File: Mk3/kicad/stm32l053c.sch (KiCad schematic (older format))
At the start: 17 parts, among them P1 SWD, U1 STM32L053C8_LQFP48, U2 ADS1015, U3 AP2112, U4 EDGE_SMA, U5 RFM92/95

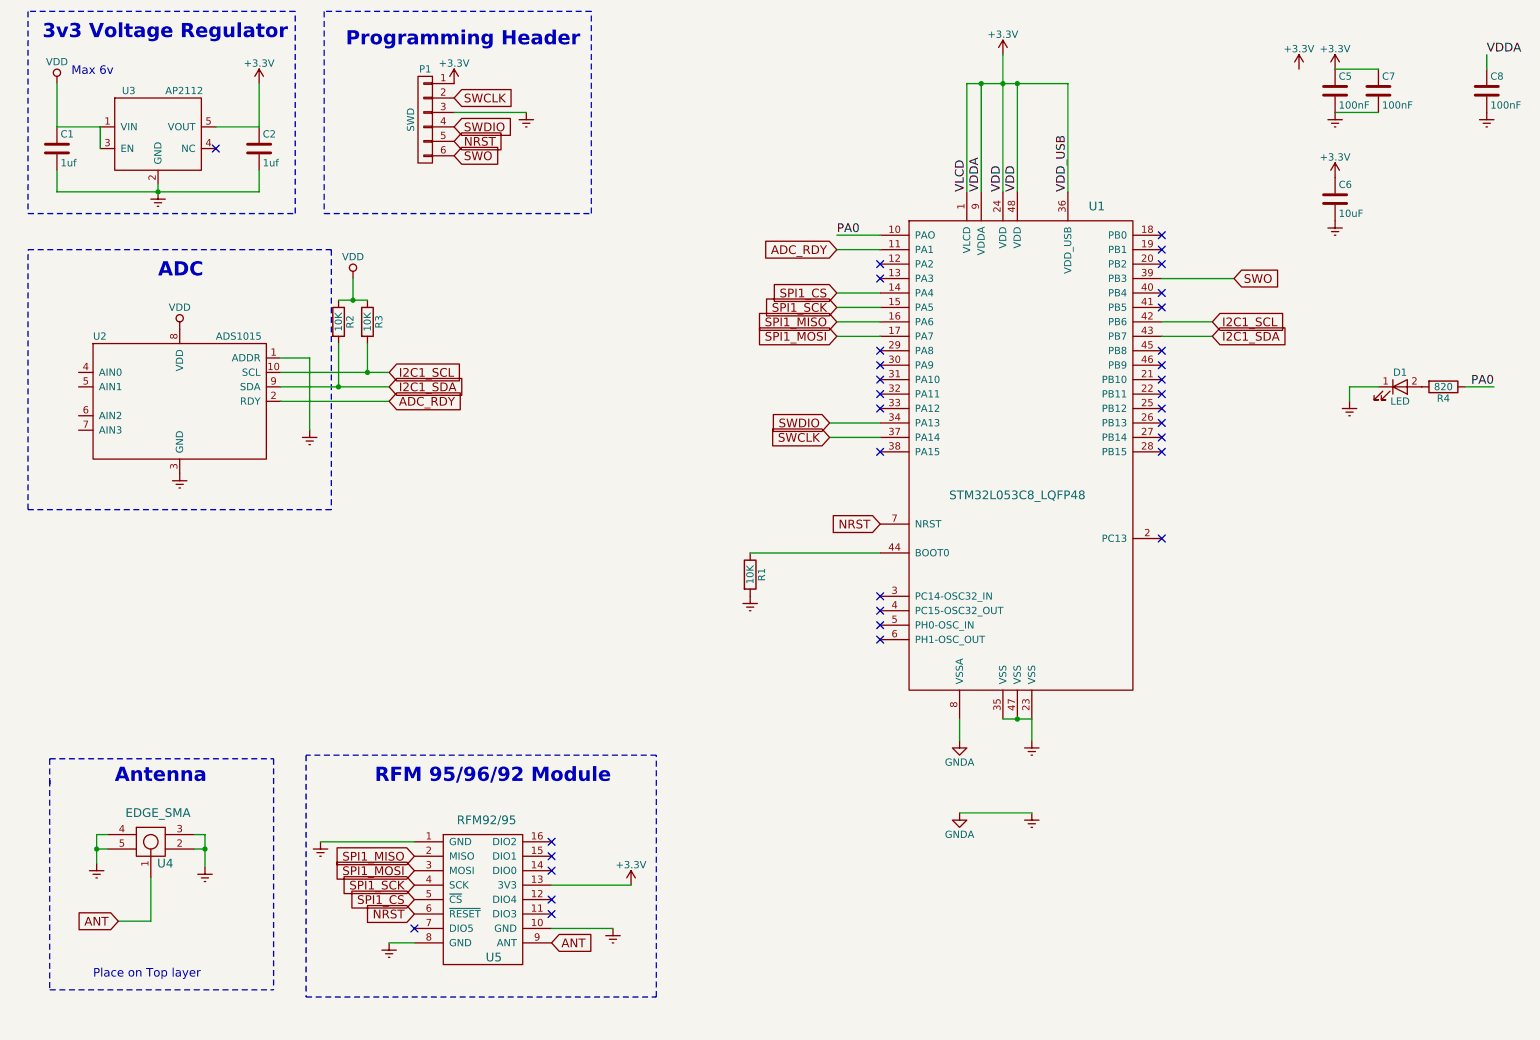
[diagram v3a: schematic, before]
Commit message: ADC connections
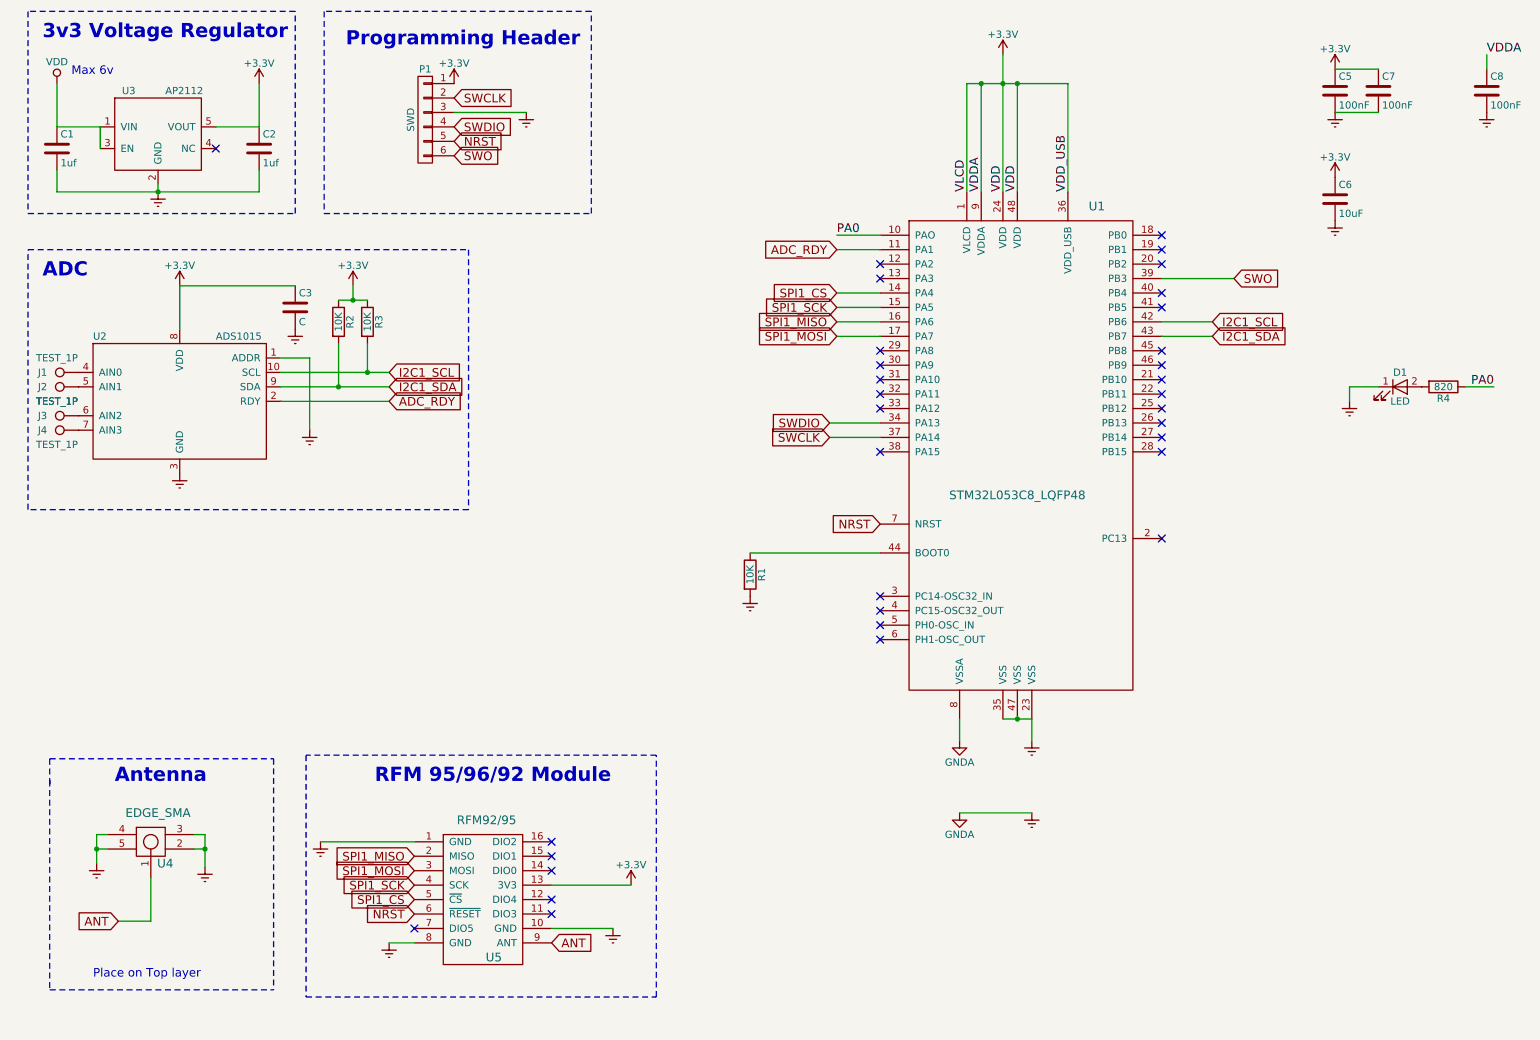
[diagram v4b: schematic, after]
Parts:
- added C3: C, symbol C
- added J1, J2, J3, J4: TEST_1P, symbol TEST_1P
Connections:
- net +3V3: now also C3.1
- net Earth: now also C3.2
- net at U2.4 (AIN0): now also J1.1
- net at U2.5 (AIN1): now also J2.1
- net at U2.6 (AIN2): now also J3.1
- net at U2.7 (AIN3): now also J4.1
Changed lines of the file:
@@
 	-1   0    0    -1
 $EndComp
-Text Notes 1450 2400 0    98   ~ 20
+Text Notes 650  2400 0    98   ~ 20
 ADC
-$Comp
-L VDD #PWR012
-U 1 1 592DF7A0
-P 1600 2750
-F 0 "#PWR012" H 1600 2600 50  0001 C CNN
-F 1 "VDD" H 1600 2900 50  0000 C CNN
-F 2 "" H 1600 2750 50  0000 C CNN
-F 3 "" H 1600 2750 50  0000 C CNN
-	1    1600 2750
-	1    0    0    -1
-$EndComp
-Wire Notes Line
-	550  2200 2650 2200
-Wire Notes Line
-	2650 2200 2650 4000
-Wire Notes Line
-	2650 4000 550  4000
+Wire Notes Line
+	550  2200 3600 2200
+Wire Notes Line
+	3600 2200 3600 4000
+Wire Notes Line
+	3600 4000 550  4000
 Wire Notes Line
 	550  4000 550  2200
@@
 3v3 Voltage Regulator
 $Comp
-L VDD #PWR013
+L VDD #PWR012
 U 1 1 592F1B4B
 P 750 1050
-F 0 "#PWR013" H 750 900 50  0001 C CNN
+F 0 "#PWR012" H 750 900 50  0001 C CNN
 F 1 "VDD" H 750 1200 50  0000 C CNN
 F 2 "" H 750 1050 50  0000 C CNN
@@
 NoConn ~ 1850 1500
 $Comp
-L Earth #PWR014
+L Earth #PWR013
 U 1 1 592F1C89
 P 1450 1800
-F 0 "#PWR014" H 1450 1550 50  0001 C CNN
+F 0 "#PWR013" H 1450 1550 50  0001 C CNN
 F 1 "Earth" H 1450 1650 50  0001 C CNN
 F 2 "" H 1450 1800 50  0000 C CNN
@@
 NRST
 $Comp
-L +3.3V #PWR015
+L +3.3V #PWR014
 U 1 1 592F43A5
 P 2150 1050
-F 0 "#PWR015" H 2150 900 50  0001 C CNN
+F 0 "#PWR014" H 2150 900 50  0001 C CNN
 F 1 "+3.3V" H 2150 1190 50  0000 C CNN
 F 2 "" H 2150 1050 50  0001 C CNN
@@
 $EndComp
 $Comp
-L +3.3V #PWR016
+L +3.3V #PWR015
 U 1 1 592F4BC3
 P 3500 1050
-F 0 "#PWR016" H 3500 900 50  0001 C CNN
+F 0 "#PWR015" H 3500 900 50  0001 C CNN
 F 1 "+3.3V" H 3500 1190 50  0000 C CNN
 F 2 "" H 3500 1050 50  0001 C CNN
@@
 $EndComp
 $Comp
-L +3.3V #PWR017
+L +3.3V #PWR016
 U 1 1 592F4E66
 P 7300 850
-F 0 "#PWR017" H 7300 700 50  0001 C CNN
+F 0 "#PWR016" H 7300 700 50  0001 C CNN
 F 1 "+3.3V" H 7300 990 50  0000 C CNN
 F 2 "" H 7300 850 50  0001 C CNN
@@
 $EndComp
 $Comp
-L +3.3V #PWR018
-U 1 1 592F5385
-P 9350 950
-F 0 "#PWR018" H 9350 800 50  0001 C CNN
-F 1 "+3.3V" H 9350 1090 50  0000 C CNN
-F 2 "" H 9350 950 50  0001 C CNN
-F 3 "" H 9350 950 50  0001 C CNN
-	1    9350 950
-	1    0    0    -1
-$EndComp
-$Comp
-L +3.3V #PWR019
+L +3.3V #PWR017
 U 1 1 592F53D7
 P 4725 6600
-F 0 "#PWR019" H 4725 6450 50  0001 C CNN
+F 0 "#PWR017" H 4725 6450 50  0001 C CNN
 F 1 "+3.3V" H 4725 6740 50  0000 C CNN
 F 2 "" H 4725 6600 50  0001 C CNN
@@
 $EndComp
 $Comp
-L +3.3V #PWR020
+L +3.3V #PWR018
 U 1 1 592F540C
 P 9600 950
-F 0 "#PWR020" H 9600 800 50  0001 C CNN
+F 0 "#PWR018" H 9600 800 50  0001 C CNN
 F 1 "+3.3V" H 9600 1090 50  0000 C CNN
 F 2 "" H 9600 950 50  0001 C CNN
@@
 $EndComp
 $Comp
-L +3.3V #PWR021
+L +3.3V #PWR019
 U 1 1 592F54CD
 P 9600 1700
-F 0 "#PWR021" H 9600 1550 50  0001 C CNN
+F 0 "#PWR019" H 9600 1550 50  0001 C CNN
 F 1 "+3.3V" H 9600 1840 50  0000 C CNN
 F 2 "" H 9600 1700 50  0001 C CNN
@@
 NoConn ~ 3225 6900
 $Comp
-L Earth #PWR022
+L Earth #PWR020
 U 1 1 592F7C8A
 P 4600 6900
-F 0 "#PWR022" H 4600 6650 50  0001 C CNN
+F 0 "#PWR020" H 4600 6650 50  0001 C CNN
 F 1 "Earth" H 4600 6750 50  0001 C CNN
 F 2 "" H 4600 6900 50  0000 C CNN
@@
 $EndComp
 $Comp
-L Earth #PWR023
+L Earth #PWR021
 U 1 1 592F7CF0
 P 2575 6300
-F 0 "#PWR023" H 2575 6050 50  0001 C CNN
+F 0 "#PWR021" H 2575 6050 50  0001 C CNN
 F 1 "Earth" H 2575 6150 50  0001 C CNN
 F 2 "" H 2575 6300 50  0000 C CNN
@@
 $EndComp
 $Comp
-L Earth #PWR024
+L Earth #PWR022
 U 1 1 592F7EE4
 P 3050 7000
-F 0 "#PWR024" H 3050 6750 50  0001 C CNN
+F 0 "#PWR022" H 3050 6750 50  0001 C CNN
 F 1 "Earth" H 3050 6850 50  0001 C CNN
 F 2 "" H 3050 7000 50  0000 C CNN
@@
 $EndComp
 $Comp
-L Earth #PWR025
+L Earth #PWR023
 U 1 1 592F80DC
 P 1025 6450
-F 0 "#PWR025" H 1025 6200 50  0001 C CNN
+F 0 "#PWR023" H 1025 6200 50  0001 C CNN
 F 1 "Earth" H 1025 6300 50  0001 C CNN
 F 2 "" H 1025 6450 50  0000 C CNN
@@
 $EndComp
 $Comp
-L Earth #PWR026
+L Earth #PWR024
 U 1 1 592F814F
 P 1775 6475
-F 0 "#PWR026" H 1775 6225 50  0001 C CNN
+F 0 "#PWR024" H 1775 6225 50  0001 C CNN
 F 1 "Earth" H 1775 6325 50  0001 C CNN
 F 2 "" H 1775 6475 50  0000 C CNN
@@
 	2300 3050 3050 3050
 Wire Wire Line
-	3050 3150 2300 3150
+	2300 3150 3050 3150
 Wire Wire Line
 	2700 2850 2700 3150
@@
 	2900 2850 2900 3050
 Connection ~ 2900 3050
-$Comp
-L VDD #PWR027
-U 1 1 593015DF
-P 2800 2400
-F 0 "#PWR027" H 2800 2250 50  0001 C CNN
-F 1 "VDD" H 2800 2550 50  0000 C CNN
-F 2 "" H 2800 2400 50  0000 C CNN
-F 3 "" H 2800 2400 50  0000 C CNN
-	1    2800 2400
-	1    0    0    -1
-$EndComp
 Wire Wire Line
 	2700 2550 2900 2550
-Wire Wire Line
-	2800 2400 2800 2550
 Connection ~ 2800 2550
 $Comp
-L Earth #PWR028
+L Earth #PWR025
 U 1 1 59301904
 P 2500 3450
-F 0 "#PWR028" H 2500 3200 50  0001 C CNN
+F 0 "#PWR025" H 2500 3200 50  0001 C CNN
 F 1 "Earth" H 2500 3300 50  0001 C CNN
 F 2 "" H 2500 3450 50  0000 C CNN
@@
 Wire Wire Line
 	1050 1500 1050 1350
+$Comp
+L TEST_1P J1
+U 1 1 59301FBF
+P 900 3050
+F 0 "J1" V 900 3300 50  0000 C CNN
+F 1 "TEST_1P" V 1000 3200 50  0000 C CNN
+F 2 "" H 1100 3050 50  0001 C CNN
+F 3 "" H 1100 3050 50  0001 C CNN
+	1    900  3050
+	0    -1   -1   0
+$EndComp
+$Comp
+L TEST_1P J2
+U 1 1 59302111
+P 900 3150
+F 0 "J2" V 900 3400 50  0000 C CNN
+F 1 "TEST_1P" V 800 3300 50  0000 C CNN
+F 2 "" H 1100 3150 50  0001 C CNN
+F 3 "" H 1100 3150 50  0001 C CNN
+	1    900  3150
+	0    -1   -1   0
+$EndComp
+$Comp
+L TEST_1P J3
+U 1 1 593021A0
+P 900 3350
+F 0 "J3" V 900 3600 50  0000 C CNN
+F 1 "TEST_1P" V 1000 3500 50  0000 C CNN
+F 2 "" H 1100 3350 50  0001 C CNN
+F 3 "" H 1100 3350 50  0001 C CNN
+	1    900  3350
+	0    -1   -1   0
+$EndComp
+$Comp
+L TEST_1P J4
+U 1 1 593021F0
+P 900 3450
+F 0 "J4" V 900 3700 50  0000 C CNN
+F 1 "TEST_1P" V 800 3600 50  0000 C CNN
+F 2 "" H 1100 3450 50  0001 C CNN
+F 3 "" H 1100 3450 50  0001 C CNN
+	1    900  3450
+	0    -1   -1   0
+$EndComp
+$Comp
+L C C3
+U 1 1 5930245B
+P 2400 2600
+F 0 "C3" H 2425 2700 50  0000 L CNN
+F 1 "C" H 2425 2500 50  0000 L CNN
+F 2 "" H 2438 2450 50  0001 C CNN
+F 3 "" H 2400 2600 50  0001 C CNN
+	1    2400 2600
+	1    0    0    -1
+$EndComp
+$Comp
+L Earth #PWR026
+U 1 1 593024E3
+P 2400 2750
+F 0 "#PWR026" H 2400 2500 50  0001 C CNN
+F 1 "Earth" H 2400 2600 50  0001 C CNN
+F 2 "" H 2400 2750 50  0000 C CNN
+F 3 "" H 2400 2750 50  0000 C CNN
+	1    2400 2750
+	-1   0    0    -1
+$EndComp
+Wire Wire Line
+	1600 2450 2400 2450
+Wire Wire Line
+	1600 2450 1600 2750
+$Comp
+L +3.3V #PWR027
+U 1 1 59303669
+P 1600 2450
+F 0 "#PWR027" H 1600 2300 50  0001 C CNN
+F 1 "+3.3V" H 1600 2590 50  0000 C CNN
+F 2 "" H 1600 2450 50  0001 C CNN
+F 3 "" H 1600 2450 50  0001 C CNN
+	1    1600 2450
+	1    0    0    -1
+$EndComp
+$Comp
+L +3.3V #PWR028
+U 1 1 59303771
+P 2800 2450
+F 0 "#PWR028" H 2800 2300 50  0001 C CNN
+F 1 "+3.3V" H 2800 2590 50  0000 C CNN
+F 2 "" H 2800 2450 50  0001 C CNN
+F 3 "" H 2800 2450 50  0001 C CNN
+	1    2800 2450
+	1    0    0    -1
+$EndComp
+Wire Wire Line
+	2800 2550 2800 2450
 $EndSCHEMATC

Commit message: Footprints
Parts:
- C1, C2, C3: footprint (none) -> Capacitors_SMD:C_0805_HandSoldering
- D1: footprint (none) -> LEDs:LED_0805
- J1, J2, J3, J4: footprint (none) -> SMD_Packages:1Pin
- R2, R3: footprint (none) -> Resistors_SMD:R_0805_HandSoldering
- U3: footprint (none) -> TO_SOT_Packages_SMD:SOT-23-5_HandSoldering
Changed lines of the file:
@@
 encoding utf-8
 Sheet 1 1
-Title "thingBot-LoRa"
-Date "2016-11-24"
-Rev "v1.1"
-Comp "thingTronics Innovations Pvt. Ltd."
-Comment1 "Approved By: Lovelesh Patel"
-Comment2 "Designed By: Manohar Bompella"
+Title "LoRa Garden Solar"
+Date ""
+Rev "v1.0.0"
+Comp ""
+Comment1 ""
+Comment2 ""
 Comment3 ""
 Comment4 ""
@@
 F 0 "D1" H 10050 3250 50  0000 C CNN
 F 1 "LED" H 10050 3050 50  0000 C CNN
-F 2 "" H 10050 3150 50  0001 C CNN
+F 2 "LEDs:LED_0805" H 10050 3150 50  0001 C CNN
 F 3 "" H 10050 3150 50  0001 C CNN
 	1    10050 3150
@@
 F 0 "U3" H 1200 1600 50  0000 L CNN
 F 1 "AP2112" H 1500 1600 50  0000 L CNN
-F 2 "" H 1400 1300 50  0001 C CNN
+F 2 "TO_SOT_Packages_SMD:SOT-23-5_HandSoldering" H 1400 1300 50  0001 C CNN
 F 3 "" H 550 1750 50  0001 C CNN
 	1    1450 1350
@@
 F 0 "R3" V 2980 2700 50  0000 C CNN
 F 1 "10K" V 2900 2700 50  0000 C CNN
-F 2 "" V 2830 2700 50  0001 C CNN
+F 2 "Resistors_SMD:R_0805_HandSoldering" V 2830 2700 50  0001 C CNN
 F 3 "" H 2900 2700 50  0001 C CNN
 	1    2900 2700
@@
 F 0 "R2" V 2780 2700 50  0000 C CNN
 F 1 "10K" V 2700 2700 50  0000 C CNN
-F 2 "" V 2630 2700 50  0001 C CNN
+F 2 "Resistors_SMD:R_0805_HandSoldering" V 2630 2700 50  0001 C CNN
 F 3 "" H 2700 2700 50  0001 C CNN
 	1    2700 2700
@@
 F 0 "C1" H 775 1600 50  0000 L CNN
 F 1 "1uf" H 775 1400 50  0000 L CNN
-F 2 "" H 788 1350 50  0001 C CNN
+F 2 "Capacitors_SMD:C_0805_HandSoldering" H 788 1350 50  0001 C CNN
 F 3 "" H 750 1500 50  0001 C CNN
 	1    750  1500
@@
 F 0 "C2" H 2175 1600 50  0000 L CNN
 F 1 "1uf" H 2175 1400 50  0000 L CNN
-F 2 "" H 2188 1350 50  0001 C CNN
+F 2 "Capacitors_SMD:C_0805_HandSoldering" H 2188 1350 50  0001 C CNN
 F 3 "" H 2150 1500 50  0001 C CNN
 	1    2150 1500
@@
 F 0 "J1" V 900 3300 50  0000 C CNN
 F 1 "TEST_1P" V 1000 3200 50  0000 C CNN
-F 2 "" H 1100 3050 50  0001 C CNN
+F 2 "SMD_Packages:1Pin" H 1100 3050 50  0001 C CNN
 F 3 "" H 1100 3050 50  0001 C CNN
 	1    900  3050
@@
 F 0 "J2" V 900 3400 50  0000 C CNN
 F 1 "TEST_1P" V 800 3300 50  0000 C CNN
-F 2 "" H 1100 3150 50  0001 C CNN
+F 2 "SMD_Packages:1Pin" H 1100 3150 50  0001 C CNN
 F 3 "" H 1100 3150 50  0001 C CNN
 	1    900  3150
@@
 F 0 "J3" V 900 3600 50  0000 C CNN
 F 1 "TEST_1P" V 1000 3500 50  0000 C CNN
-F 2 "" H 1100 3350 50  0001 C CNN
+F 2 "SMD_Packages:1Pin" H 1100 3350 50  0001 C CNN
 F 3 "" H 1100 3350 50  0001 C CNN
 	1    900  3350
@@
 F 0 "J4" V 900 3700 50  0000 C CNN
 F 1 "TEST_1P" V 800 3600 50  0000 C CNN
-F 2 "" H 1100 3450 50  0001 C CNN
+F 2 "SMD_Packages:1Pin" H 1100 3450 50  0001 C CNN
 F 3 "" H 1100 3450 50  0001 C CNN
 	1    900  3450
@@
 F 0 "C3" H 2425 2700 50  0000 L CNN
 F 1 "C" H 2425 2500 50  0000 L CNN
-F 2 "" H 2438 2450 50  0001 C CNN
+F 2 "Capacitors_SMD:C_0805_HandSoldering" H 2438 2450 50  0001 C CNN
 F 3 "" H 2400 2600 50  0001 C CNN
 	1    2400 2600

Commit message: ADC footprint
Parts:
- U2: footprint (none) -> Housings_SSOP:TSSOP-10_3x3mm_Pitch0.5mm
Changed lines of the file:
@@
 F 0 "U2" H 1000 3700 50  0000 L CNN
 F 1 "ADS1015" H 1850 3700 50  0000 L CNN
-F 2 "" H 1550 3200 50  0001 C CNN
+F 2 "Housings_SSOP:TSSOP-10_3x3mm_Pitch0.5mm" H 1550 3200 50  0001 C CNN
 F 3 "" H 700 3650 50  0001 C CNN
 	1    1600 3250

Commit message: Start of layout
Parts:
- added J5: CONN_BATT, Pin_Headers:Pin_Header_Straight_1x02_Pitch2.54mm, symbol CONN_01X02
- U4: footprint sma:EDGE_SMA_5 -> kicad:EDGE_SMA_5
- U5: footprint Temp:RFM92_95_96_98 -> kicad:RFM92_95_96_98
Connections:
- net labels added: +BATT
- wire segments 61 -> 64
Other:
- note added: "Debug LED"
- note added: "Power"
- note removed: "3v3 Voltage Regulator"
- moved on the sheet: C1, C2, C3, C5, C6, C7, C8, D1, J1, J2, J3, J4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

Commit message: Initial layout
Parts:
- removed J1, J2, J3, J4: TEST_1P, SMD_Packages:1Pin, symbol TEST_1P
- removed J5: CONN_BATT, Pin_Headers:Pin_Header_Straight_1x02_Pitch2.54mm, symbol CONN_01X02
- added BT1: Battery, Pin_Headers:Pin_Header_Straight_1x02_Pitch2.54mm, symbol Battery
- added J1: CONN_01X04, Pin_Headers:Pin_Header_Straight_1x04_Pitch2.54mm, symbol CONN_01X04
- P1: footprint Pin_Headers:Pin_Header_Straight_1x06 -> Pin_Headers:Pin_Header_Straight_1x06_Pitch2.54mm
- renumbered C5 to C1, C7 to C2, C8 to C3, C6 to C4, C1 to C5, C2 to C6, C3 to C7, R4 to R1, R1 to R4, U3 to U1, U1 to U2, U2 to U3
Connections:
- wire segments 64 -> 75
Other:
- moved on the sheet: C7, R2, R3, U3
